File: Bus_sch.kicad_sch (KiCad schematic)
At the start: 6 parts

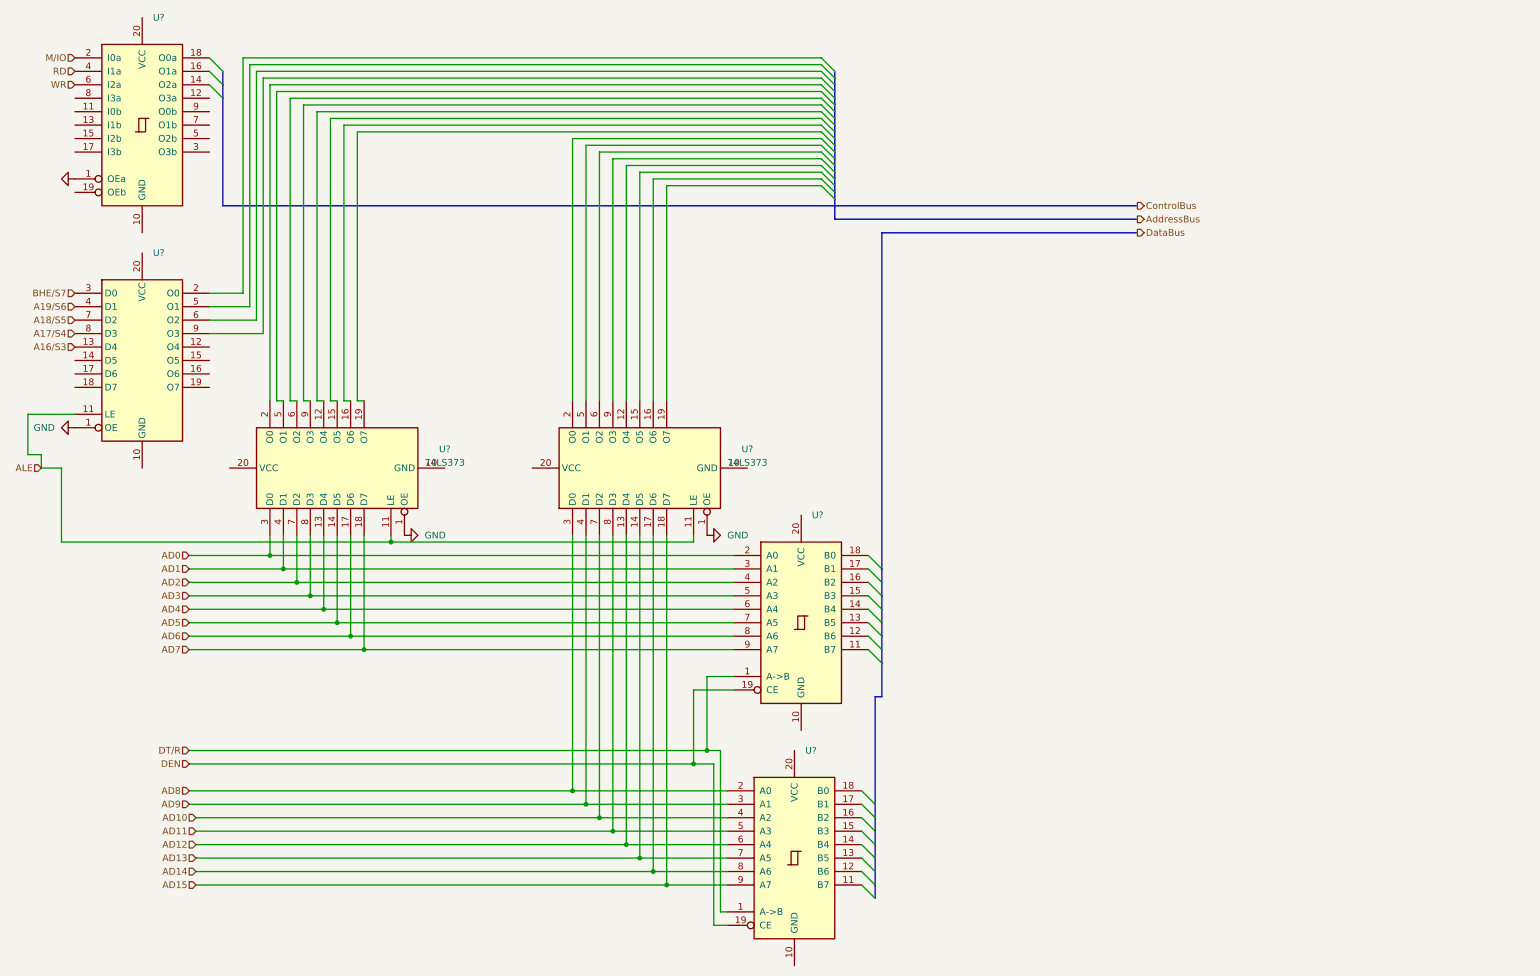
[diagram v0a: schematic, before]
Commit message: Added headers to the necessary pins, and created IO device sheet
Added headers for the three chips and for the busses. Also created and started to address  decode the actual IO components.
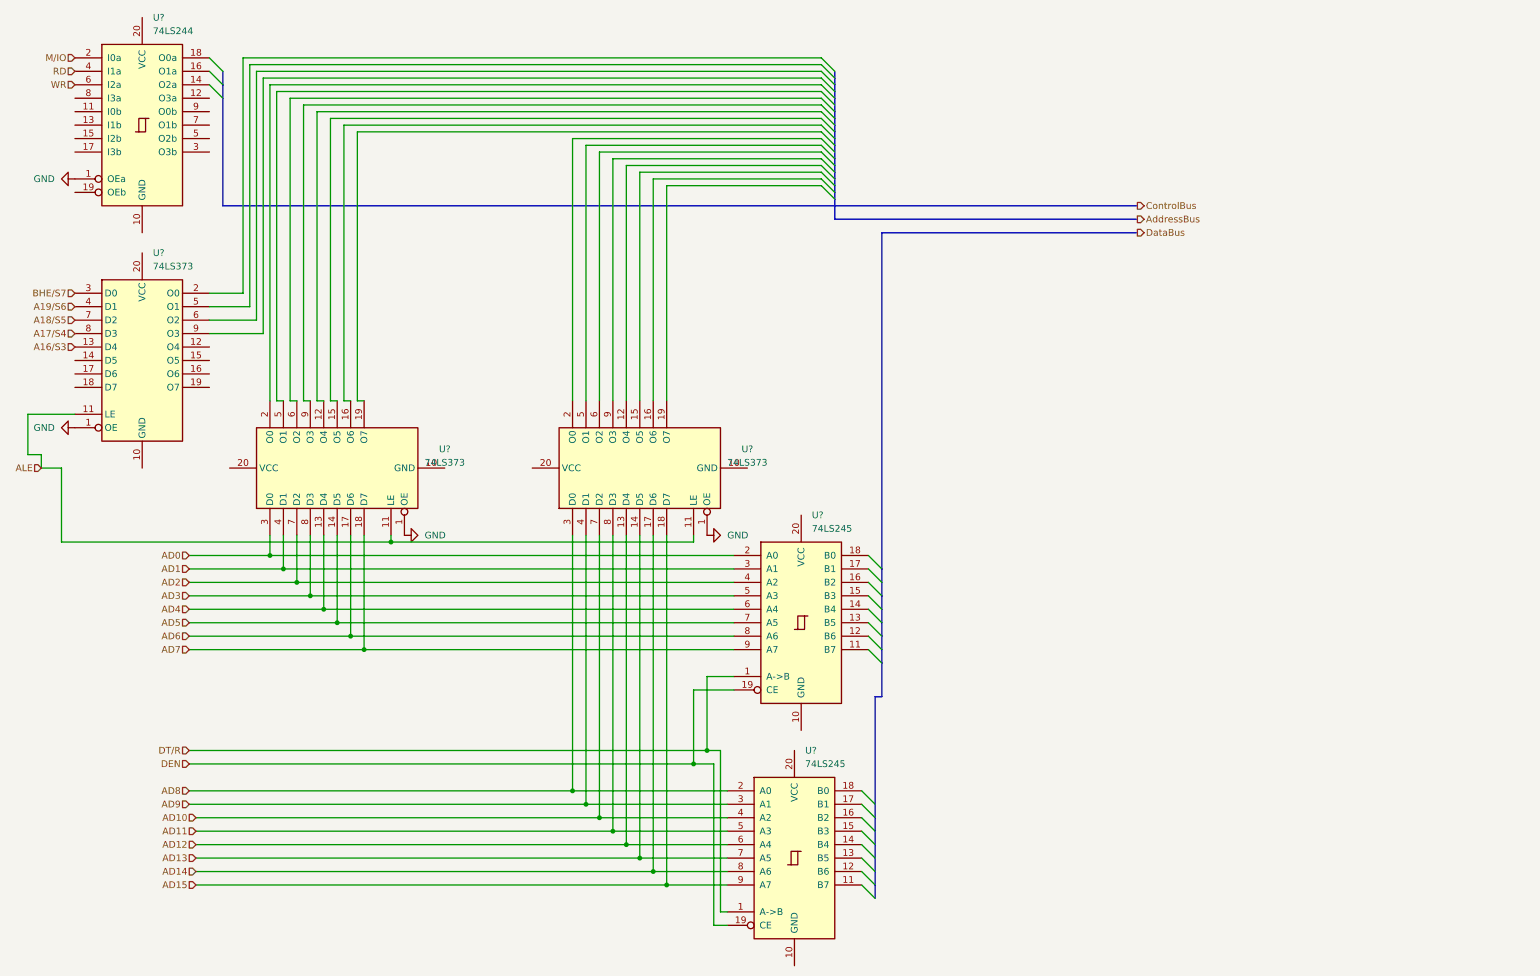
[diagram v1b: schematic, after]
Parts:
- U?: value (none) -> 74LS373
- U? (x2): value (none) -> 74LS245
- U?: value (none) -> 74LS244
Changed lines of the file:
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@@
       (effects (font (size 1.27 1.27)) (justify left))
     )
-    (property "Value" "" (id 1) (at 38.8494 57.15 0)
+    (property "Value" "74LS373" (id 1) (at 38.8494 57.15 0)
       (effects (font (size 1.27 1.27)) (justify left))
     )
@@
       (effects (font (size 1.27 1.27)) hide)
     )
-    (property "Value" "" (id 1) (at 20.32 40.6399 90)
+    (property "Value" "GND" (id 1) (at 20.32 40.6399 90)
       (effects (font (size 1.27 1.27)) (justify right))
     )
@@
       (effects (font (size 1.27 1.27)) (justify left))
     )
-    (property "Value" "" (id 1) (at 163.3094 106.68 0)
+    (property "Value" "74LS245" (id 1) (at 163.3094 106.68 0)
       (effects (font (size 1.27 1.27)) (justify left))
     )
@@
       (effects (font (size 1.27 1.27)) (justify left))
     )
-    (property "Value" "" (id 1) (at 162.0394 151.13 0)
+    (property "Value" "74LS245" (id 1) (at 162.0394 151.13 0)
       (effects (font (size 1.27 1.27)) (justify left))
     )
@@
       (effects (font (size 1.27 1.27)) (justify left))
     )
-    (property "Value" "" (id 1) (at 38.8494 12.7 0)
-      (effects (font (size 1.27 1.27)) (justify left))
-    )
+    (property "Value" "74LS244" (id 1) (at 38.8494 12.7 0)
+      (effects (font (size 1.27 1.27)) (justify left))
+    )

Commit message: Moved Bus headers
Moved the bus headers to the sheet with the decoding to save space
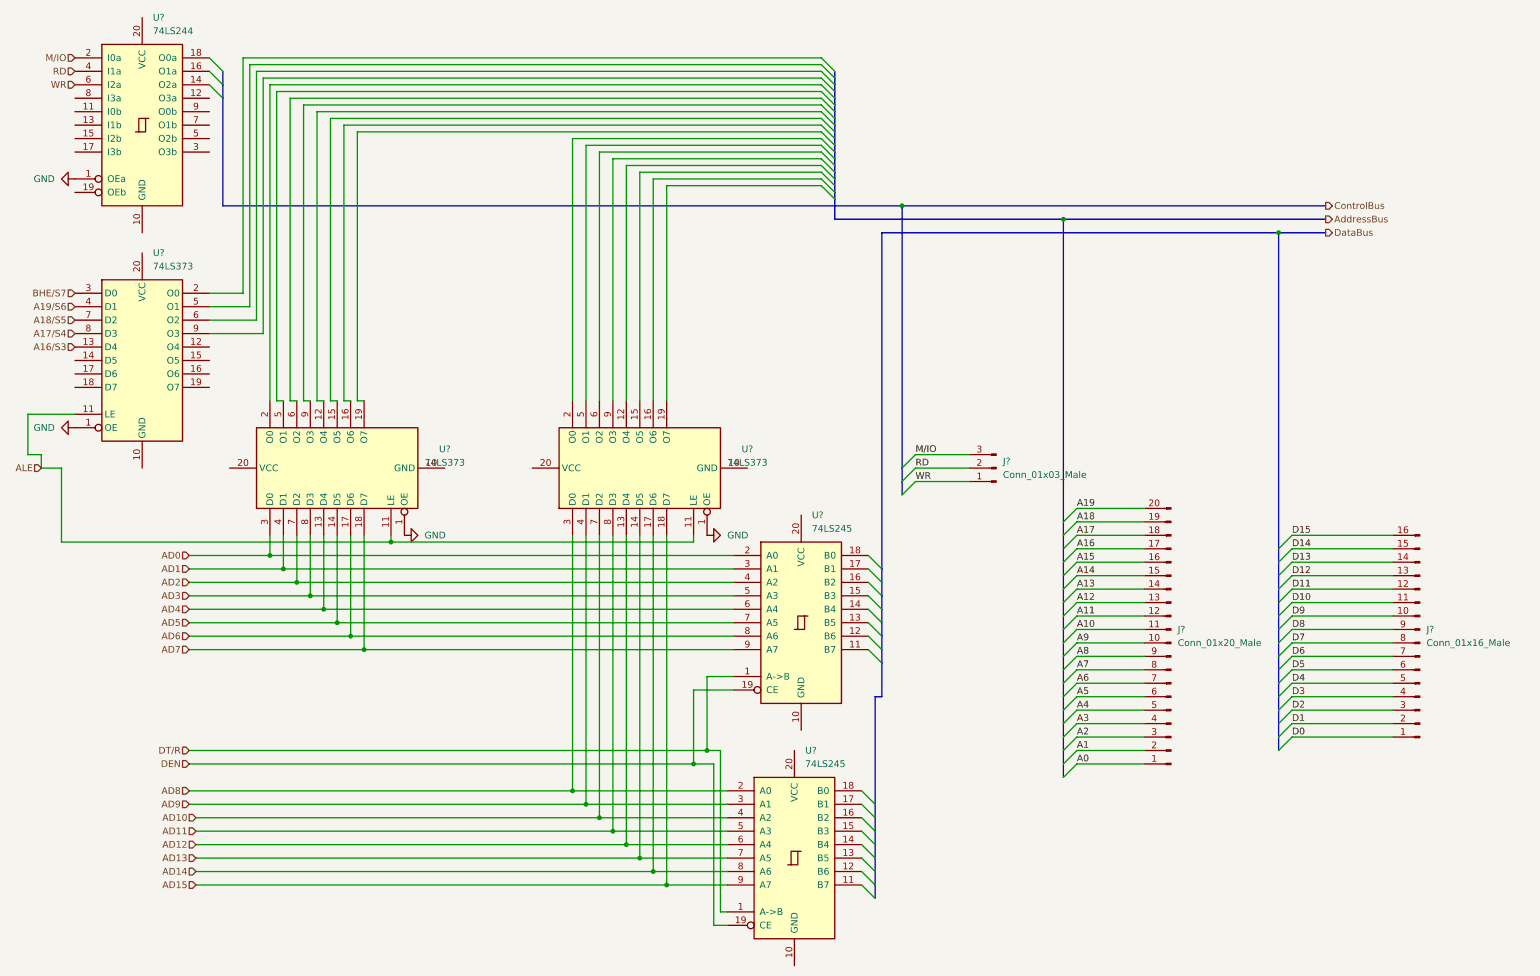
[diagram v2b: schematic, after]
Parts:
- added J?: Conn_01x16_Male, symbol Connector:Conn_01x16_Male
- added J?: Conn_01x20_Male, symbol Connector:Conn_01x20_Male
- added J?: Conn_01x03_Male, symbol Connector:Conn_01x03_Male
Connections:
- net M/IO: now also J?.3 (Pin_3)
- net RD: now also J?.2 (Pin_2)
- net WR: now also J?.1 (Pin_1)
- new net A0: J?.1 (Pin_1)
- new net A1: J?.2 (Pin_2)
- new net A10: J?.11 (Pin_11)
- new net A11: J?.12 (Pin_12)
- new net A12: J?.13 (Pin_13)
- new net A13: J?.14 (Pin_14)
- new net A14: J?.15 (Pin_15)
- new net A15: J?.16 (Pin_16)
- new net A16: J?.17 (Pin_17)
- new net A17: J?.18 (Pin_18)
- new net A18: J?.19 (Pin_19)
- new net A19: J?.20 (Pin_20)
- new net A2: J?.3 (Pin_3)
- new net A3: J?.4 (Pin_4)
- new net A4: J?.5 (Pin_5)
- new net A5: J?.6 (Pin_6)
- new net A6: J?.7 (Pin_7)
- new net A7: J?.8 (Pin_8)
- new net A8: J?.9 (Pin_9)
- new net A9: J?.10 (Pin_10)
- new net D0: J?.1 (Pin_1)
- new net D1: J?.2 (Pin_2)
- new net D10: J?.11 (Pin_11)
- new net D11: J?.12 (Pin_12)
- new net D12: J?.13 (Pin_13)
- new net D13: J?.14 (Pin_14)
- new net D14: J?.15 (Pin_15)
- new net D15: J?.16 (Pin_16)
- new net D2: J?.3 (Pin_3)
- new net D3: J?.4 (Pin_4)
- new net D4: J?.5 (Pin_5)
- new net D5: J?.6 (Pin_6)
- new net D6: J?.7 (Pin_7)
- new net D7: J?.8 (Pin_8)
- new net D8: J?.9 (Pin_9)
- new net D9: J?.10 (Pin_10)

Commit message: Wired Push Buttons and added footprints
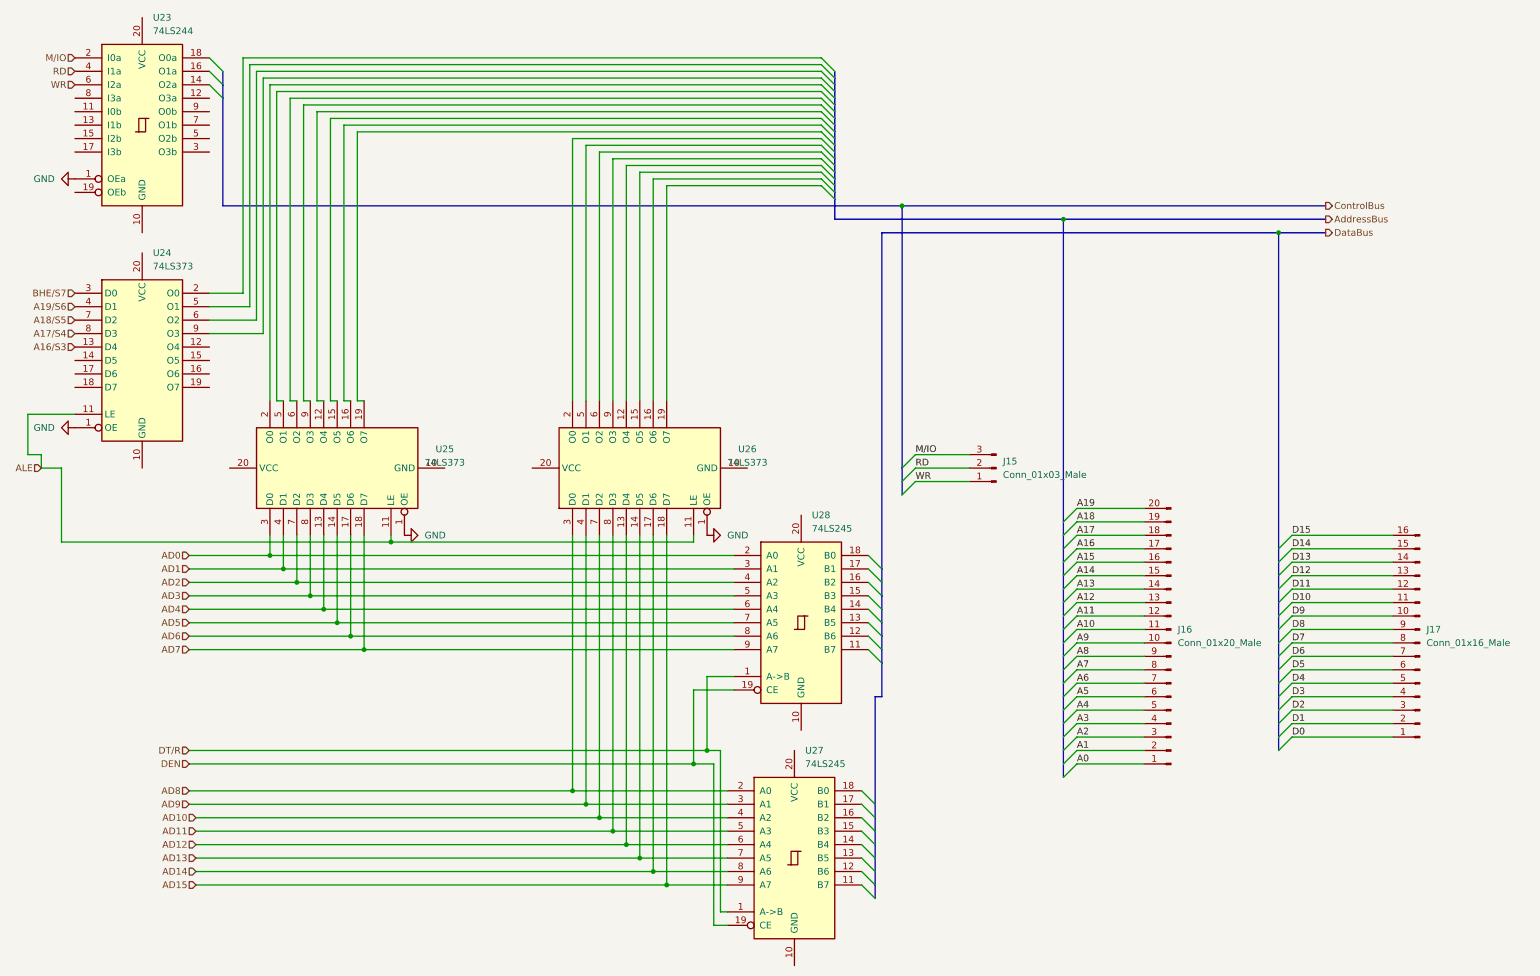
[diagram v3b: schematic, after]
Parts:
- gave numbers to parts that had none: 9
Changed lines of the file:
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@@
   (symbol (lib_id "74xx:74LS373") (at 36.83 74.93 0) (unit 1)
     (in_bom yes) (on_board yes) (fields_autoplaced)
-    (property "Reference" "U?" (id 0) (at 38.8494 54.61 0)
+    (property "Reference" "U24" (id 0) (at 38.8494 54.61 0)
       (effects (font (size 1.27 1.27)) (justify left))
     )
@@
   (symbol (lib_id "power:GND") (at 143.51 107.95 90) (unit 1)
     (in_bom yes) (on_board yes) (fields_autoplaced)
-    (property "Reference" "#PWR?" (id 0) (at 149.86 107.95 0)
+    (property "Reference" "#PWR0117" (id 0) (at 149.86 107.95 0)
       (effects (font (size 1.27 1.27)) hide)
     )
@@
   (symbol (lib_id "power:GND") (at 24.13 40.64 270) (unit 1)
     (in_bom yes) (on_board yes) (fields_autoplaced)
-    (property "Reference" "#PWR?" (id 0) (at 17.78 40.64 0)
+    (property "Reference" "#PWR0116" (id 0) (at 17.78 40.64 0)
       (effects (font (size 1.27 1.27)) hide)
     )
@@
   (symbol (lib_id "power:GND") (at 86.36 107.95 90) (unit 1)
     (in_bom yes) (on_board yes) (fields_autoplaced)
-    (property "Reference" "#PWR?" (id 0) (at 92.71 107.95 0)
+    (property "Reference" "#PWR0114" (id 0) (at 92.71 107.95 0)
       (effects (font (size 1.27 1.27)) hide)
     )
@@
   (symbol (lib_id "74xx:74LS373") (at 130.81 95.25 90) (unit 1)
     (in_bom yes) (on_board yes) (fields_autoplaced)
-    (property "Reference" "U?" (id 0) (at 151.13 91.6686 90))
+    (property "Reference" "U26" (id 0) (at 151.13 91.6686 90))
     (property "Value" "74LS373" (id 1) (at 151.13 94.2086 90))
     (property "Footprint" "" (id 2) (at 130.81 95.25 0)
@@
   (symbol (lib_id "power:GND") (at 24.13 87.63 270) (unit 1)
     (in_bom yes) (on_board yes) (fields_autoplaced)
-    (property "Reference" "#PWR?" (id 0) (at 17.78 87.63 0)
+    (property "Reference" "#PWR0115" (id 0) (at 17.78 87.63 0)
       (effects (font (size 1.27 1.27)) hide)
     )
@@
   (symbol (lib_id "74xx:74LS245") (at 161.29 124.46 0) (unit 1)
     (in_bom yes) (on_board yes) (fields_autoplaced)
-    (property "Reference" "U?" (id 0) (at 163.3094 104.14 0)
+    (property "Reference" "U28" (id 0) (at 163.3094 104.14 0)
       (effects (font (size 1.27 1.27)) (justify left))
     )
@@
   (symbol (lib_id "Connector:Conn_01x16_Male") (at 278.13 128.27 180) (unit 1)
     (in_bom yes) (on_board yes) (fields_autoplaced)
-    (property "Reference" "J?" (id 0) (at 279.4 125.7299 0)
+    (property "Reference" "J17" (id 0) (at 279.4 125.7299 0)
       (effects (font (size 1.27 1.27)) (justify right))
     )
@@
   (symbol (lib_id "Connector:Conn_01x20_Male") (at 231.14 128.27 180) (unit 1)
     (in_bom yes) (on_board yes) (fields_autoplaced)
-    (property "Reference" "J?" (id 0) (at 232.41 125.7299 0)
+    (property "Reference" "J16" (id 0) (at 232.41 125.7299 0)
       (effects (font (size 1.27 1.27)) (justify right))
     )
@@
   (symbol (lib_id "74xx:74LS373") (at 73.66 95.25 90) (unit 1)
     (in_bom yes) (on_board yes) (fields_autoplaced)
-    (property "Reference" "U?" (id 0) (at 93.98 91.6686 90))
+    (property "Reference" "U25" (id 0) (at 93.98 91.6686 90))
     (property "Value" "74LS373" (id 1) (at 93.98 94.2086 90))
     (property "Footprint" "" (id 2) (at 73.66 95.25 0)
@@
   (symbol (lib_id "74xx:74LS245") (at 160.02 168.91 0) (unit 1)
     (in_bom yes) (on_board yes) (fields_autoplaced)
-    (property "Reference" "U?" (id 0) (at 162.0394 148.59 0)
+    (property "Reference" "U27" (id 0) (at 162.0394 148.59 0)
       (effects (font (size 1.27 1.27)) (justify left))
     )
@@
   (symbol (lib_id "Connector:Conn_01x03_Male") (at 198.12 95.25 180) (unit 1)
     (in_bom yes) (on_board yes) (fields_autoplaced)
-    (property "Reference" "J?" (id 0) (at 199.39 93.9799 0)
+    (property "Reference" "J15" (id 0) (at 199.39 93.9799 0)
       (effects (font (size 1.27 1.27)) (justify right))
     )
@@
   (symbol (lib_id "74xx:74LS244") (at 36.83 30.48 0) (unit 1)
     (in_bom yes) (on_board yes) (fields_autoplaced)
-    (property "Reference" "U?" (id 0) (at 38.8494 10.16 0)
-      (effects (font (size 1.27 1.27)) (justify left))
-    )
+    (property "Reference" "U23" (id 0) (at 38.8494 10.16 0)
+      (effects (font (size 1.27 1.27)) (justify left))
+    )
